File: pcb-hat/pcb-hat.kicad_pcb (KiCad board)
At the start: 4 copper layers, 40.9 x 60.1 mm, 69 parts, among them Q1 Q_PMOS_GSD, Q2 Q_NPN, Q3 PJA3404A_R1_00001, Q4 2N7002K_R1_00001, U1 Headers, U2 INA219AxD, U3 HTD Servo, U4 TL431DBZ, U5 AP63300WU-7, U7 AP63300WU-7, U8 Raspberry_Pi_Generic

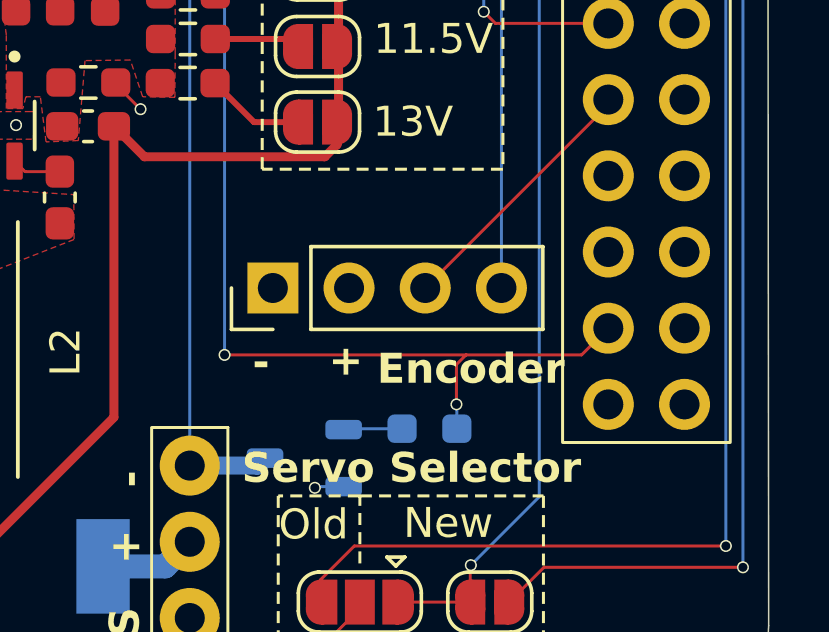
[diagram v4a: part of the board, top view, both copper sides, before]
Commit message: Add silkscreen for encoder and buzzer
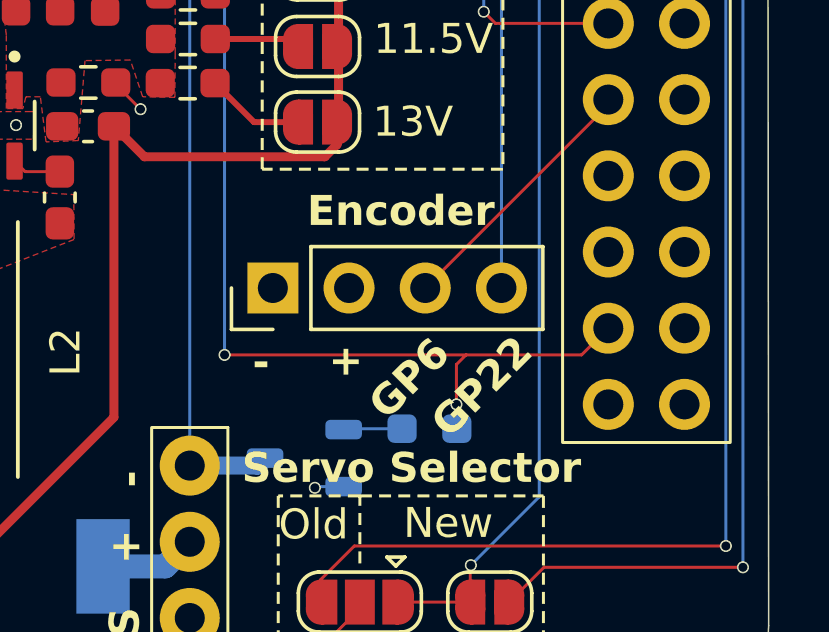
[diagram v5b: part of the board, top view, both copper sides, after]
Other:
- board text added: "Drive GPIO 5 High"
- board text added: "GP22"
- board text added: "GP6"
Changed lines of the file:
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@@
 		)
 	)
+	(gr_text "GP6"
+		(at 139.4 114.36 45)
+		(layer "F.SilkS")
+		(effects
+			(font
+				(size 1 1)
+				(thickness 0.2)
+				(bold yes)
+			)
+			(justify left bottom)
+		)
+	)
 	(gr_text "-"
 		(at 116.02 64.39 0)
@@
 	)
 	(gr_text "Encoder"
-		(at 139 113.12 0)
+		(at 136.67 107.86 0)
 		(layer "F.SilkS")
 		(effects
@@
 		)
 	)
+	(gr_text "GP22"
+		(at 141.48 114.97 45)
+		(layer "F.SilkS")
+		(effects
+			(font
+				(size 1 1)
+				(thickness 0.2)
+				(bold yes)
+			)
+			(justify left bottom)
+		)
+	)
+	(gr_text "Drive GPIO 5 High"
+		(at 141.63 95.42 0)
+		(layer "B.SilkS")
+		(effects
+			(font
+				(size 1 1)
+				(thickness 0.2)
+				(bold yes)
+			)
+			(justify left bottom mirror)
+		)
+	)
 	(table
 		(column_count 2)
@@
 		(polygon
 			(pts
-				(xy 112.15 62.88) (xy 121.69 62.9) (xy 121.49 69.11) (xy 113.14 69.86) (xy 113.23 71.74) (xy 111.59 72.2)
+				(xy 112.15 62.88) (xy 121.69 62.9) (xy 117.44 67.01) (xy 113.14 69.86) (xy 113.23 71.74) (xy 111.59 72.2)
 				(xy 112.13 65.93)
 			)
@@
 		)
 	)
+	(group ""
+		(members "1c09e1a8-8c98-4183-98ce-24670e4685ee" "261cb890-0711-4fba-9f3c-227d757f646b"
+			"ebe54c5d-0e88-4e7b-b02e-5a422b7d2819"
+		)
+	)

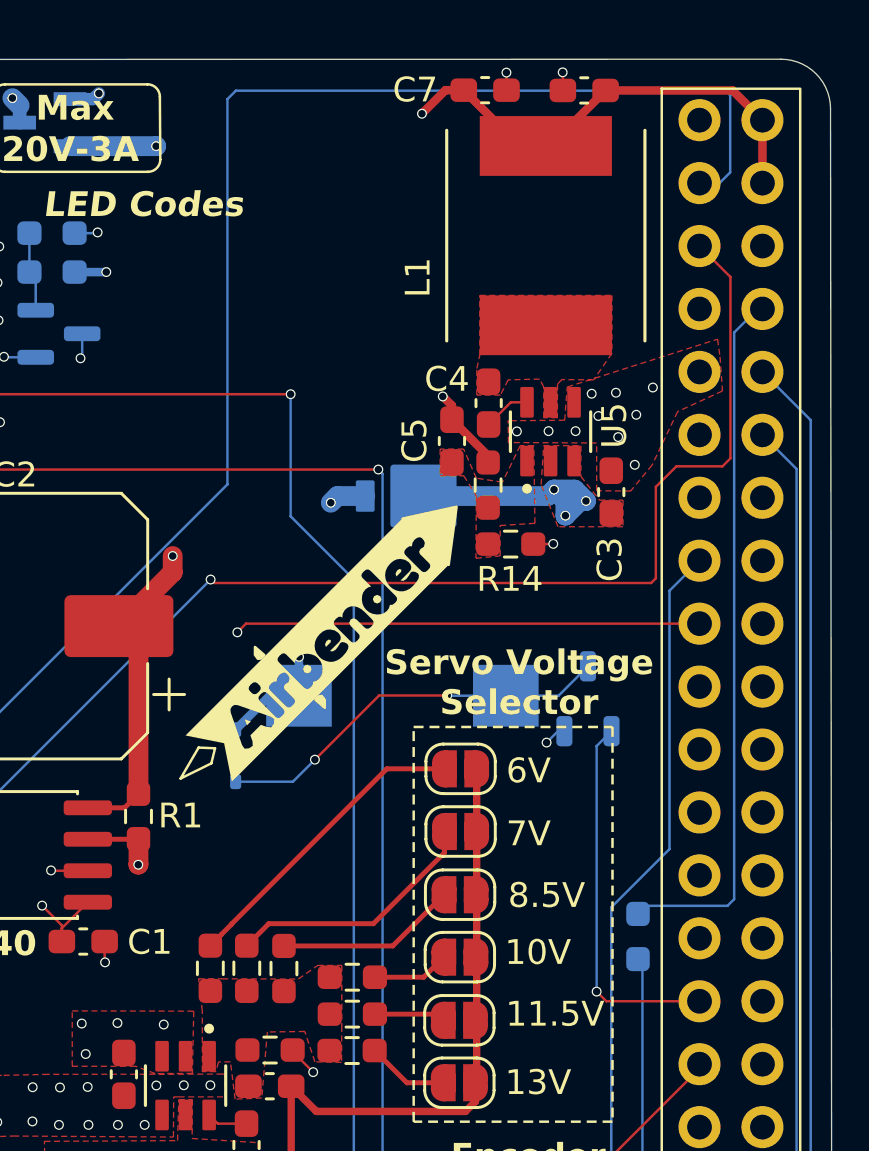
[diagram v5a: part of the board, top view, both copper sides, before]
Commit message: Revert back to using 3.3V and no flyback for buzzer
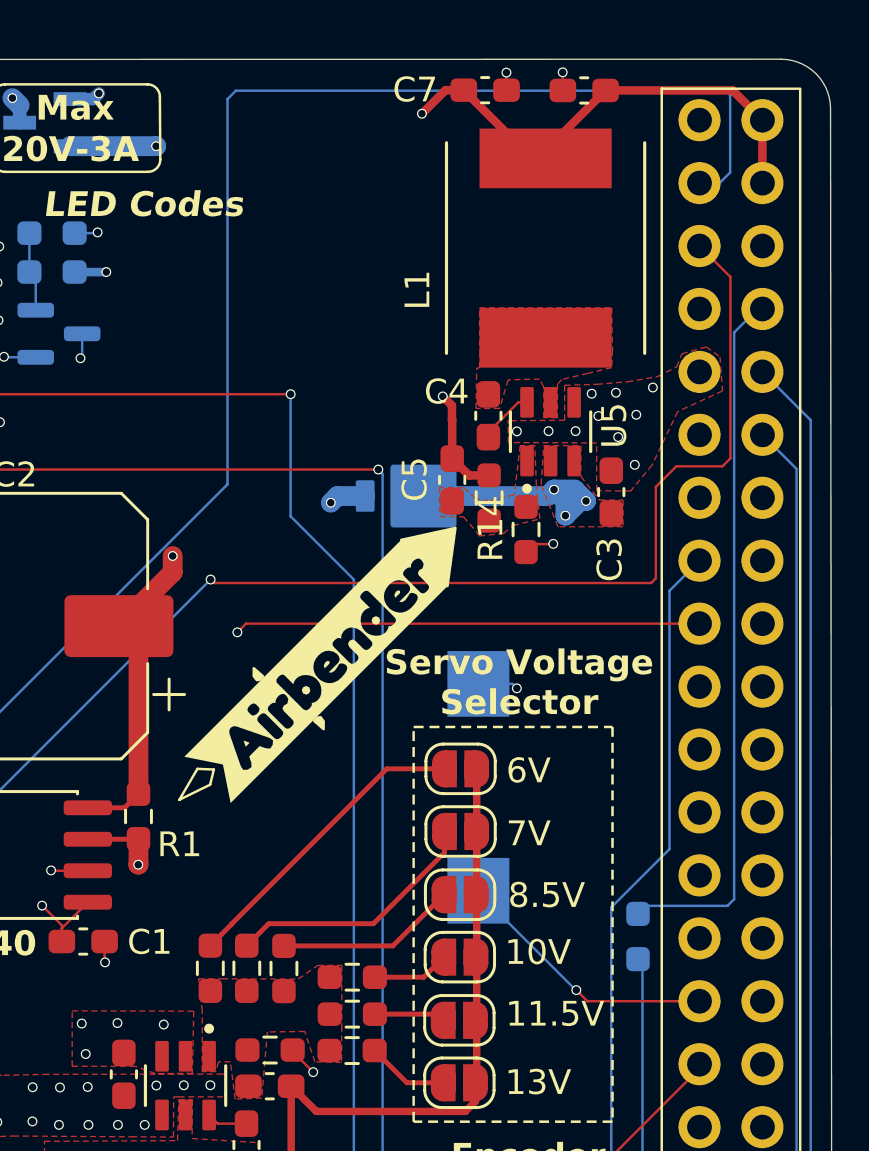
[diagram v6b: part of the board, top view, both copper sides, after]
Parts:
- removed D6: 1N4148WS, Diode_SMD:D_SOD-323
- removed Q4: 2N7002K_R1_00001, Package_TO_SOT_SMD:TSOT-23
- U5, U7: value AP63300WU-7 -> AP63301WU-7
- moved LS1 4.80 mm to (137.8, 92.4), turned to -90 degrees
- moved G*** 3.76 mm to (122.3, 100.8)
- moved C5 1.57 mm to (136.7, 80.0)
- moved kibuzzard-694E41B7 0.86 mm to (131.5, 87.4)
- moved R14 0.86 mm to (139.7, 82.0), turned to -90 degrees
- moved R13 0.52 mm to (138.2, 80.7)
- moved C4 0.51 mm to (138.2, 77.4)
- moved L1 0.50 mm to (140.5, 70.6)
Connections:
- LS1 pad 1: +5V -> /GPIO5
- LS1 pad 2: Net-(D6-A) -> GND
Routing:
- net Net-(D6-A): track 16.2 -> 0.00 mm, vias 2 -> 0
- net +5V: track 115.1 -> 106.3 mm, vias 5 -> 4
- net /GPIO5: track 15.1 -> 10.7 mm
- net GND: track 24.1 -> 25.1 mm
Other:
- board text added: "Buzzer"

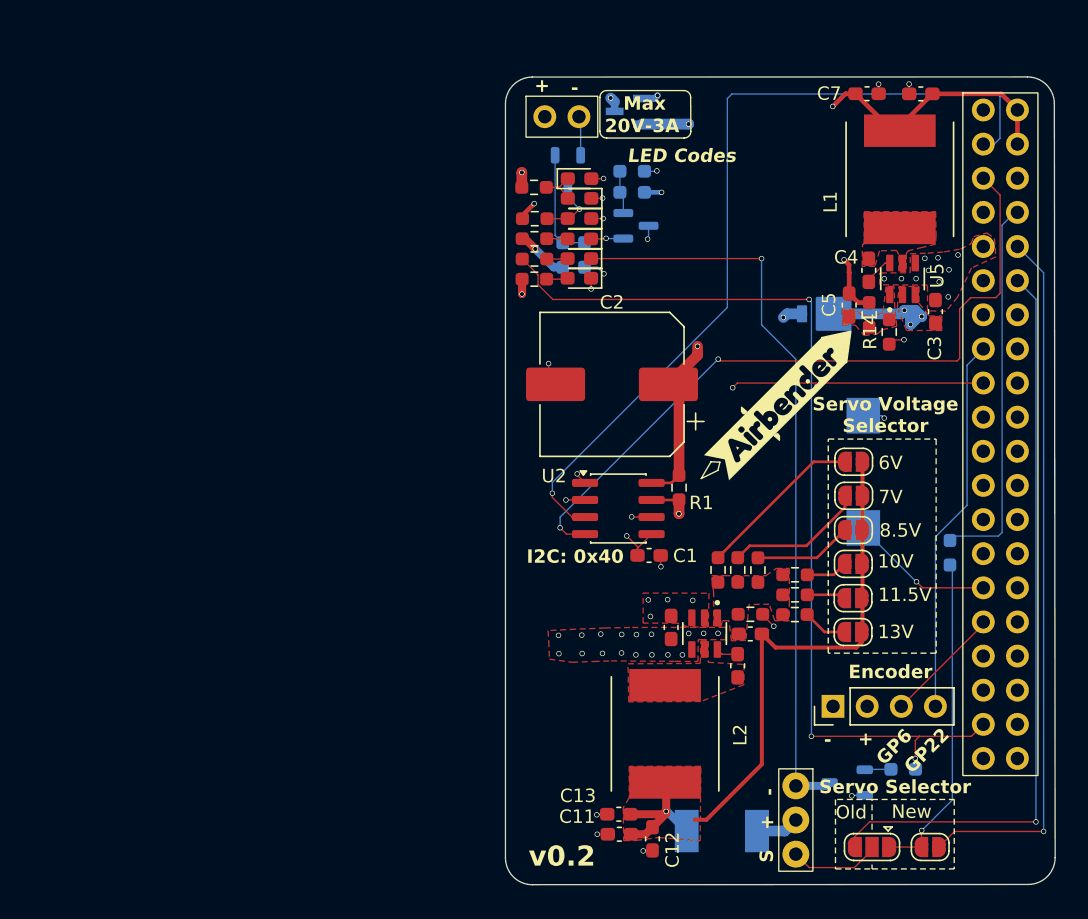
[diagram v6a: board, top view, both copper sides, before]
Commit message: Add gnd pour on B.Cu, change default trace thickness to 0.2mm
Also make the SW node to the inductor slightly closer
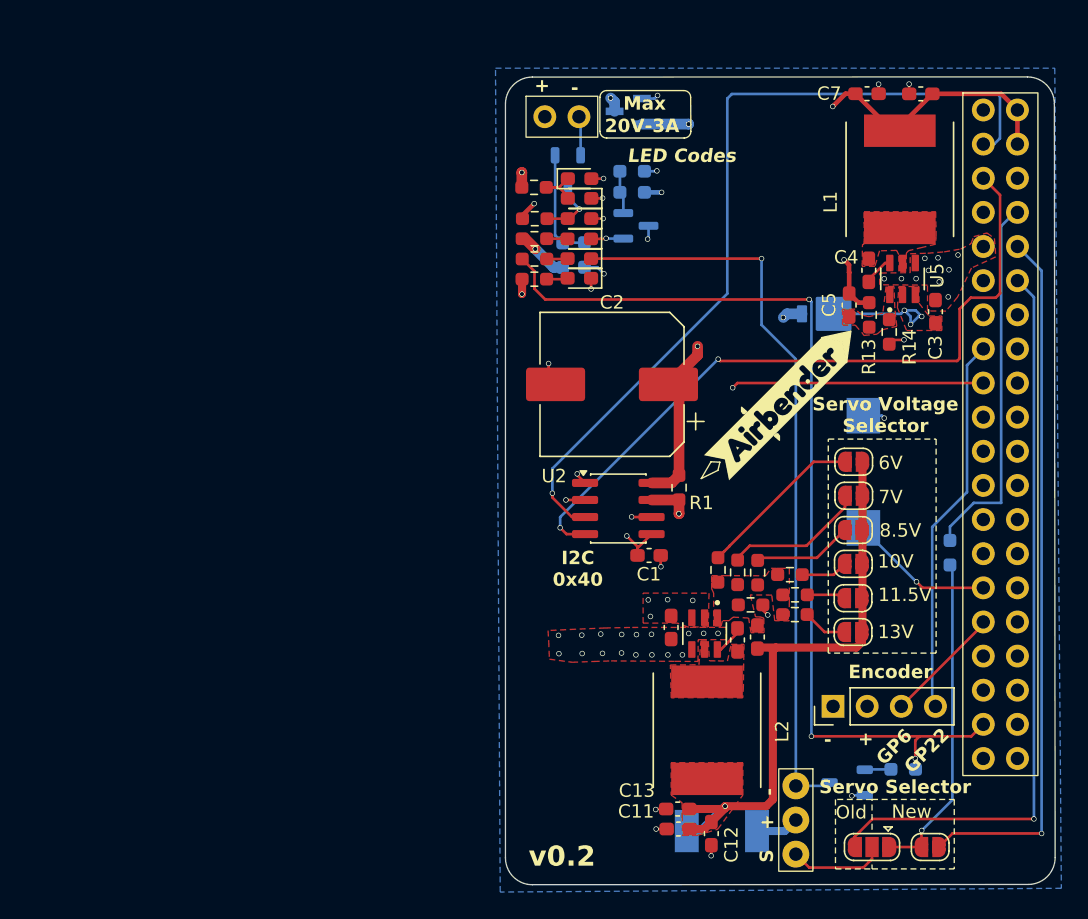
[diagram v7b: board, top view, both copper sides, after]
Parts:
- moved C11 4.40 mm to (124.0, 119.0)
- moved C12 4.40 mm to (126.5, 119.3)
- moved C13 4.40 mm to (124.0, 117.5)
- moved L2 3.13 mm to (126.2, 111.6)
- moved C9 1.92 mm to (128.4, 104.9)
- moved R15 0.70 mm to (129.4, 102.3)
- moved C10 0.58 mm to (129.9, 104.7), turned to 90 degrees
- moved R19 0.38 mm to (132.3, 100.0)
- moved R18 0.19 mm to (129.9, 99.9)
- moved R17 0.18 mm to (128.4, 99.9)
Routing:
- net VDC: track 94.2 -> 98.6 mm
- net Net-(U7-BST): track 1.65 -> 2.35 mm
- added copper zone on B.Cu, net GND
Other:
- board text added: "I2C 0x40"
- board text removed: "I2C: 0x40"
